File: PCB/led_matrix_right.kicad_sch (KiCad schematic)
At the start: 42 parts

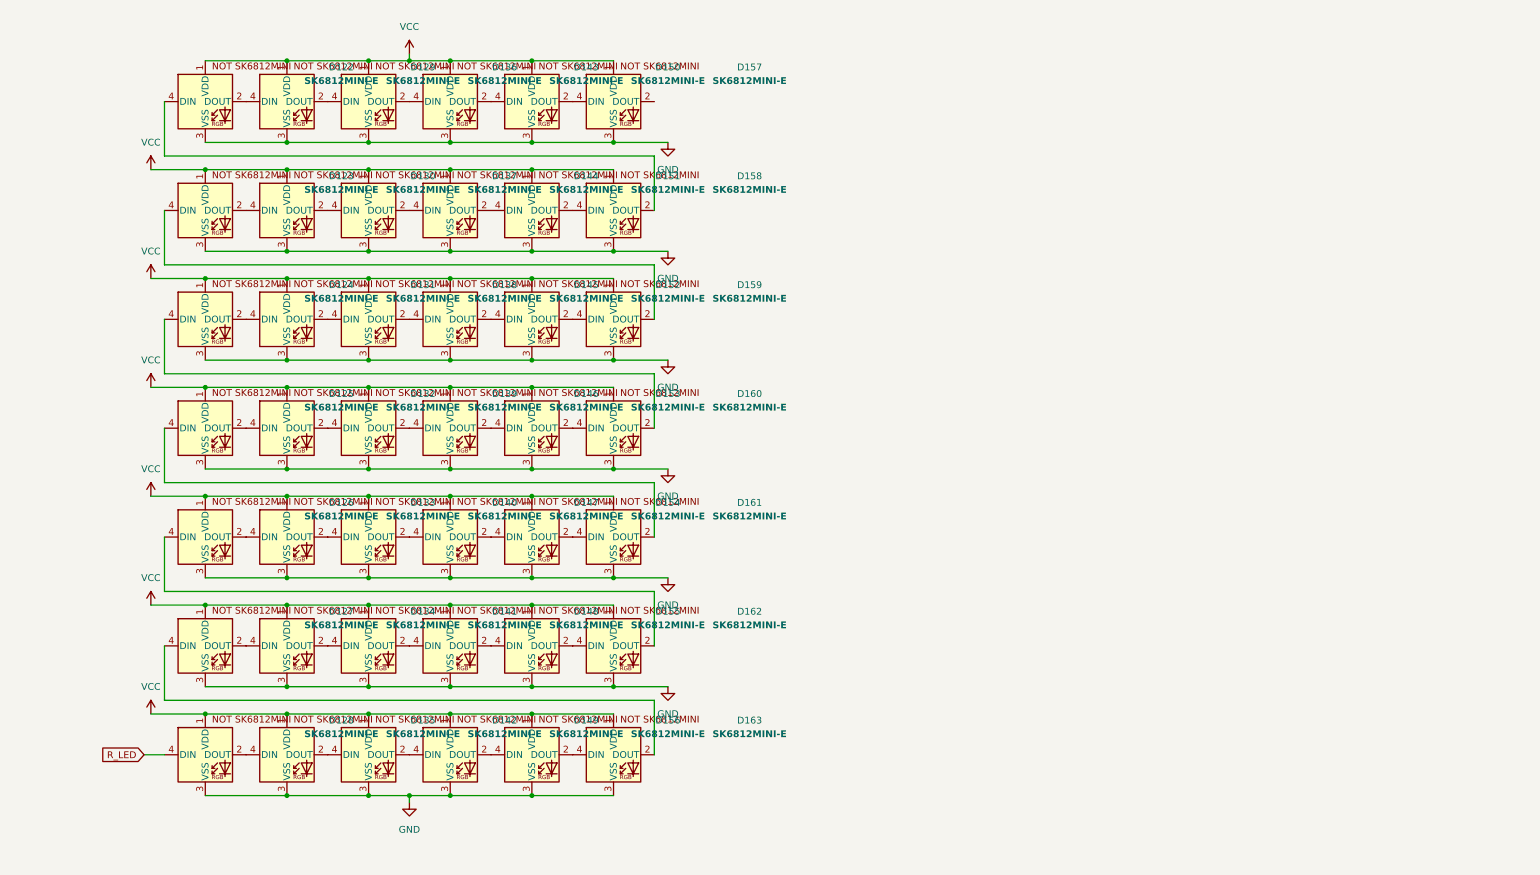
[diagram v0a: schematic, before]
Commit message: routed the switches and diodes
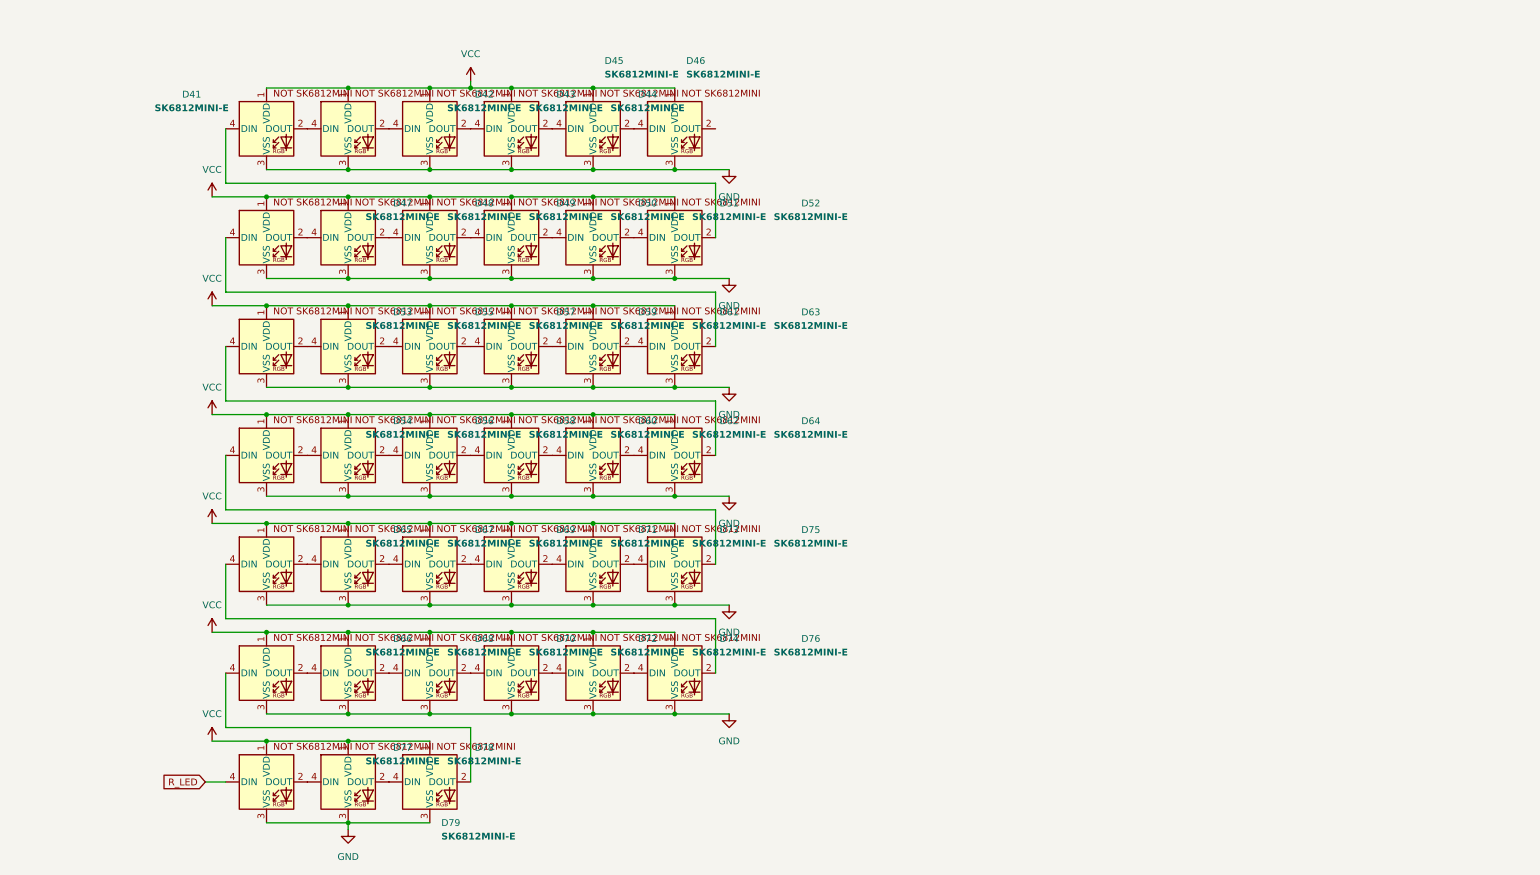
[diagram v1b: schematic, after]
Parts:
- removed D122, D123, D124, D125, D126, D127, D128, D129, D130, D131, D132, D133, D134, D135, D136, D137, D138, D139, D140, D141, D142, D143, D144, D145, D146, D147, D148, D149, D150, D151, D152, D153, D154, D155, D156, D157, D158, D159, D160, D161, D162, D163: SK6812MINI-E, footprints:SK6812MINI-E_fixed, symbol SK6812MINI-E:SK6812MINI-E
- added D41, D42, D43, D44, D45, D46, D47, D48, D49, D50, D51, D52, D53, D54, D55, D56, D57, D58, D59, D60, D61, D62, D63, D64, D65, D66, D67, D68, D69, D70, D71, D72, D73, D74, D75, D76, D77, D78, D79: SK6812MINI-E, footprints:SK6812MINI-E_fixed, symbol SK6812MINI-E:SK6812MINI-E
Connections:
- net GND: now also D41.3 (VSS), D42.3 (VSS), D43.3 (VSS), D44.3 (VSS), D45.3 (VSS), D46.3 (VSS), D47.3 (VSS), D48.3 (VSS), D49.3 (VSS), D50.3 (VSS), D51.3 (VSS), D52.3 (VSS), D53.3 (VSS), D54.3 (VSS), D55.3 (VSS), D56.3 (VSS), D57.3 (VSS), D58.3 (VSS), D59.3 (VSS), D60.3 (VSS), D61.3 (VSS), D62.3 (VSS), D63.3 (VSS), D64.3 (VSS), D65.3 (VSS), D66.3 (VSS), D67.3 (VSS), D68.3 (VSS), D69.3 (VSS), D70.3 (VSS), D71.3 (VSS), D72.3 (VSS), D73.3 (VSS), D74.3 (VSS), D75.3 (VSS), D76.3 (VSS), D77.3 (VSS), D78.3 (VSS), D79.3 (VSS)
- net R_LED: now also D77.4 (DIN)
- net VCC: now also D41.1 (VDD), D42.1 (VDD), D43.1 (VDD), D44.1 (VDD), D45.1 (VDD), D46.1 (VDD), D47.1 (VDD), D48.1 (VDD), D49.1 (VDD), D50.1 (VDD), D51.1 (VDD), D52.1 (VDD), D53.1 (VDD), D54.1 (VDD), D55.1 (VDD), D56.1 (VDD), D57.1 (VDD), D58.1 (VDD), D59.1 (VDD), D60.1 (VDD), D61.1 (VDD), D62.1 (VDD), D63.1 (VDD), D64.1 (VDD), D65.1 (VDD), D66.1 (VDD), D67.1 (VDD), D68.1 (VDD), D69.1 (VDD), D70.1 (VDD), D71.1 (VDD), D72.1 (VDD), D73.1 (VDD), D74.1 (VDD), D75.1 (VDD), D76.1 (VDD), D77.1 (VDD), D78.1 (VDD), D79.1 (VDD)
- new net: D66.2 (DOUT), D68.4 (DIN)
- new net: D66.4 (DIN), D79.2 (DOUT)
- new net: D65.4 (DIN), D76.2 (DOUT)
- new net: D74.2 (DOUT), D76.4 (DIN)
- new net: D71.2 (DOUT), D73.4 (DIN)
- new net: D69.2 (DOUT), D71.4 (DIN)
- new net: D62.2 (DOUT), D64.4 (DIN)
- new net: D60.2 (DOUT), D62.4 (DIN)
- new net: D78.2 (DOUT), D79.4 (DIN)
- new net: D47.2 (DOUT), D48.4 (DIN)
- new net: D47.4 (DIN), D63.2 (DOUT)
- new net: D53.4 (DIN), D64.2 (DOUT)
- new net: D70.2 (DOUT), D72.4 (DIN)
- new net: D68.2 (DOUT), D70.4 (DIN)
- new net: D73.2 (DOUT), D75.4 (DIN)
- new net: D67.2 (DOUT), D69.4 (DIN)
- new net: D61.2 (DOUT), D63.4 (DIN)
- new net: D58.2 (DOUT), D60.4 (DIN)
- new net: D56.2 (DOUT), D58.4 (DIN)
- new net: D55.2 (DOUT), D57.4 (DIN)
- new net: D53.2 (DOUT), D55.4 (DIN)
- new net: D59.2 (DOUT), D61.4 (DIN)
- new net: D57.2 (DOUT), D59.4 (DIN)
- new net: D45.2 (DOUT), D46.4 (DIN)
- new net: D44.2 (DOUT), D45.4 (DIN)
- new net: D43.2 (DOUT), D44.4 (DIN)
- new net: D72.2 (DOUT), D74.4 (DIN)
- new net: D54.2 (DOUT), D56.4 (DIN)
- new net: D42.2 (DOUT), D43.4 (DIN)
- new net: D41.2 (DOUT), D42.4 (DIN)
- new net: D49.2 (DOUT), D50.4 (DIN)
- new net: D48.2 (DOUT), D49.4 (DIN)
- new net: D41.4 (DIN), D52.2 (DOUT)
- new net: D51.2 (DOUT), D52.4 (DIN)
- new net: D65.2 (DOUT), D67.4 (DIN)
- new net: D77.2 (DOUT), D78.4 (DIN)
- new net: D54.4 (DIN), D75.2 (DOUT)
- new net: D50.2 (DOUT), D51.4 (DIN)

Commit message: redid the leds
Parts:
- removed D79: SK6812MINI-E, footprints:SK6812MINI-E_fixed, symbol SK6812MINI-E:SK6812MINI-E
- D41, D42, D43, D44, D45, D46, D47, D48, D49, D50, D51, D52, D53, D54, D55, D56, D57, D58, D59, D60, D61, D62, D63, D64, D65, D66, D67, D68, D69, D70, D71, D72, D73, D74, D75, D76, D77, D78: footprint footprints:SK6812MINI-E_fixed -> SK6812MINI-E - 3.2x2.8x1.78mm
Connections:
- net R_LED: now also D41.4 (DIN); no longer D77.4 (DIN)
- net at D66.2 (DOUT): now also D67.4 (DIN); no longer D68.4 (DIN)
- net at D66.4 (DIN): now also D65.2 (DOUT)
- net at D76.2 (DOUT): now also D77.4 (DIN); no longer D65.4 (DIN)
- net at D74.2 (DOUT): now also D75.4 (DIN); no longer D76.4 (DIN)
- net at D71.2 (DOUT): now also D72.4 (DIN); no longer D73.4 (DIN)
- net at D71.4 (DIN): now also D70.2 (DOUT); no longer D69.2 (DOUT)
- net at D64.4 (DIN): now also D63.2 (DOUT); no longer D62.2 (DOUT)
- net at D62.4 (DIN): now also D61.2 (DOUT); no longer D60.2 (DOUT)
- net at D47.4 (DIN): now also D46.2 (DOUT); no longer D63.2 (DOUT)
- net at D53.4 (DIN): now also D52.2 (DOUT); no longer D64.2 (DOUT)
- net at D70.4 (DIN): now also D69.2 (DOUT); no longer D68.2 (DOUT)
- net at D73.2 (DOUT): now also D74.4 (DIN); no longer D75.4 (DIN)
- net at D67.2 (DOUT): now also D68.4 (DIN); no longer D69.4 (DIN)
- net at D63.4 (DIN): now also D62.2 (DOUT); no longer D61.2 (DOUT)
- net at D58.2 (DOUT): now also D59.4 (DIN); no longer D60.4 (DIN)
- net at D56.2 (DOUT): now also D57.4 (DIN); no longer D58.4 (DIN)
- net at D55.2 (DOUT): now also D56.4 (DIN); no longer D57.4 (DIN)
- net at D55.4 (DIN): now also D54.2 (DOUT); no longer D53.2 (DOUT)
- net at D61.4 (DIN): now also D60.2 (DOUT); no longer D59.2 (DOUT)
- net at D57.2 (DOUT): now also D58.4 (DIN); no longer D59.4 (DIN)
- net at D72.2 (DOUT): now also D73.4 (DIN); no longer D74.4 (DIN)
- net at D75.2 (DOUT): now also D76.4 (DIN); no longer D54.4 (DIN)
- new net: D53.2 (DOUT), D54.4 (DIN)
- new net: D64.2 (DOUT), D65.4 (DIN)
- new net: D59.2 (DOUT), D60.4 (DIN)
- new net: D68.2 (DOUT), D69.4 (DIN)
- no-connect marks 0 -> 1

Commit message: "finished" right side
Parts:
- added D156: SK6812MINI-E, footprints:SK6812MINI-E_fixed, symbol SK6812MINI-E:SK6812MINI-E
- D41, D42, D43, D44, D45, D46, D47, D48, D49, D50, D51, D52, D53, D54, D55, D56, D57, D58, D59, D60, D61, D62, D63, D64, D65, D66, D67, D68, D69, D70, D71, D72, D73, D74, D75, D76, D77, D78: footprint SK6812MINI-E - 3.2x2.8x1.78mm -> footprints:SK6812MINI-E_fixed
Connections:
- net GND: now also D156.3 (VSS)
- net VCC: now also D156.1 (VDD)
- net at D78.2 (DOUT): now also D156.4 (DIN)
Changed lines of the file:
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@@
 	)
 	(junction
+		(at 125.73 62.23)
+		(diameter 0)
+		(color 0 0 0 0)
+	)
+	(junction
 		(at 140.97 16.51)
 		(diameter 0)
@@
 	)
 	(junction
+		(at 110.49 77.47)
+		(diameter 0)
+		(color 0 0 0 0)
+	)
+	(junction
 		(at 217.17 54.61)
 		(diameter 0)
@@
 	)
 	(no_connect
-		(at 118.11 69.85)
+		(at 133.35 69.85)
 	)
 	(wire
@@
 	(wire
 		(pts
+			(xy 125.73 62.23) (xy 110.49 62.23)
+		)
+		(stroke
+			(width 0)
+			(type default)
+		)
+	)
+	(wire
+		(pts
 			(xy 34.29 31.75) (xy 24.13 31.75)
 		)
@@
 	(wire
 		(pts
-			(xy 273.05 62.23) (xy 110.49 62.23)
+			(xy 273.05 62.23) (xy 125.73 62.23)
 		)
 		(stroke
@@
 	(wire
 		(pts
+			(xy 110.49 77.47) (xy 125.73 77.47)
+		)
+		(stroke
+			(width 0)
+			(type default)
+		)
+	)
+	(wire
+		(pts
 			(xy 171.45 39.37) (xy 186.69 39.37)
 		)
@@
 			)
 		)
-		(property "Footprint" "SK6812MINI-E - 3.2x2.8x1.78mm"
+		(property "Footprint" "footprints:SK6812MINI-E_fixed"
 			(at 111.76 77.47 0)
 			(effects
@@
 			)
 		)
-		(property "Footprint" "SK6812MINI-E - 3.2x2.8x1.78mm"
+		(property "Footprint" "footprints:SK6812MINI-E_fixed"
 			(at 264.16 31.75 0)
 			(effects
@@
 			)
 		)
-		(property "Footprint" "SK6812MINI-E - 3.2x2.8x1.78mm"
+		(property "Footprint" "footprints:SK6812MINI-E_fixed"
 			(at 50.8 54.61 0)
 			(effects
@@
 			)
 		)
-		(property "Footprint" "SK6812MINI-E - 3.2x2.8x1.78mm"
+		(property "Footprint" "footprints:SK6812MINI-E_fixed"
 			(at 66.04 31.75 0)
 			(effects
@@
 			)
 		)
-		(property "Footprint" "SK6812MINI-E - 3.2x2.8x1.78mm"
+		(property "Footprint" "footprints:SK6812MINI-E_fixed"
 			(at 111.76 31.75 0)
 			(effects
@@
 			)
 		)
-		(property "Footprint" "SK6812MINI-E - 3.2x2.8x1.78mm"
+		(property "Footprint" "footprints:SK6812MINI-E_fixed"
 			(at 96.52 54.61 0)
 			(effects
@@
 			)
 		)
-		(property "Footprint" "SK6812MINI-E - 3.2x2.8x1.78mm"
+		(property "Footprint" "footprints:SK6812MINI-E_fixed"
 			(at 142.24 31.75 0)
 			(effects
@@
 			)
 		)
-		(property "Footprint" "SK6812MINI-E - 3.2x2.8x1.78mm"
+		(property "Footprint" "footprints:SK6812MINI-E_fixed"
 			(at 157.48 31.75 0)
 			(effects
@@
 			)
 		)
-		(property "Footprint" "SK6812MINI-E - 3.2x2.8x1.78mm"
+		(property "Footprint" "footprints:SK6812MINI-E_fixed"
 			(at 96.52 31.75 0)
 			(effects
@@
 			)
 		)
-		(property "Footprint" "SK6812MINI-E - 3.2x2.8x1.78mm"
+		(property "Footprint" "footprints:SK6812MINI-E_fixed"
 			(at 35.56 31.75 0)
 			(effects
@@
 			)
 		)
-		(property "Footprint" "SK6812MINI-E - 3.2x2.8x1.78mm"
+		(property "Footprint" "footprints:SK6812MINI-E_fixed"
 			(at 50.8 77.47 0)
 			(effects
@@
 			)
 		)
-		(property "Footprint" "SK6812MINI-E - 3.2x2.8x1.78mm"
+		(property "Footprint" "footprints:SK6812MINI-E_fixed"
 			(at 81.28 77.47 0)
 			(effects
@@
 			)
 		)
-		(property "Footprint" "SK6812MINI-E - 3.2x2.8x1.78mm"
+		(property "Footprint" "footprints:SK6812MINI-E_fixed"
 			(at 248.92 54.61 0)
 			(effects
@@
 			)
 		)
-		(property "Footprint" "SK6812MINI-E - 3.2x2.8x1.78mm"
+		(property "Footprint" "footprints:SK6812MINI-E_fixed"
 			(at 203.2 31.75 0)
 			(effects
@@
 			)
 		)
-		(property "Footprint" "SK6812MINI-E - 3.2x2.8x1.78mm"
+		(property "Footprint" "footprints:SK6812MINI-E_fixed"
 			(at 233.68 31.75 0)
 			(effects
@@
 			)
 		)
-		(property "Footprint" "SK6812MINI-E - 3.2x2.8x1.78mm"
+		(property "Footprint" "footprints:SK6812MINI-E_fixed"
 			(at 50.8 31.75 0)
 			(effects
@@
 			)
 		)
-		(property "Footprint" "SK6812MINI-E - 3.2x2.8x1.78mm"
+		(property "Footprint" "footprints:SK6812MINI-E_fixed"
 			(at 35.56 77.47 0)
 			(effects
@@
 			)
 		)
-		(property "Footprint" "SK6812MINI-E - 3.2x2.8x1.78mm"
+		(property "Footprint" "footprints:SK6812MINI-E_fixed"
 			(at 142.24 54.61 0)
 			(effects
@@
 			)
 		)
-		(property "Footprint" "SK6812MINI-E - 3.2x2.8x1.78mm"
+		(property "Footprint" "footprints:SK6812MINI-E_fixed"
 			(at 233.68 54.61 0)
 			(effects
@@
 			)
 		)
-		(property "Footprint" "SK6812MINI-E - 3.2x2.8x1.78mm"
+		(property "Footprint" "footprints:SK6812MINI-E_fixed"
 			(at 81.28 54.61 0)
 			(effects
@@
 			)
 		)
-		(property "Footprint" "SK6812MINI-E - 3.2x2.8x1.78mm"
+		(property "Footprint" "footprints:SK6812MINI-E_fixed"
 			(at 218.44 31.75 0)
 			(effects
@@
 			)
 		)
-		(property "Footprint" "SK6812MINI-E - 3.2x2.8x1.78mm"
+		(property "Footprint" "footprints:SK6812MINI-E_fixed"
 			(at 81.28 31.75 0)
 			(effects
@@
 			)
 		)
-		(property "Footprint" "SK6812MINI-E - 3.2x2.8x1.78mm"
+		(property "Footprint" "footprints:SK6812MINI-E_fixed"
 			(at 35.56 54.61 0)
 			(effects
@@
 	(symbol
 		(lib_id "SK6812MINI-E:SK6812MINI-E")
+		(at 125.73 69.85 0)
+		(unit 1)
+		(exclude_from_sim no)
+		(in_bom yes)
+		(on_board yes)
+		(dnp no)
+		(property "Reference" "D156"
+			(at 151.638 63.5 0)
+			(effects
+				(font
+					(size 1.27 1.27)
+				)
+			)
+		)
+		(property "Value" "SK6812MINI-E"
+			(at 151.13 65.9699 0)
+			(effects
+				(font
+					(size 1.27 1.27)
+					(thickness 0.254)
+					(bold yes)
+				)
+			)
+		)
+		(property "Footprint" "footprints:SK6812MINI-E_fixed"
+			(at 127 77.47 0)
+			(effects
+				(font
+					(size 1.27 1.27)
+				)
+				(justify left top)
+				(hide yes)
+			)
+		)
+		(property "Datasheet" "https://cdn-shop.adafruit.com/product-files/4960/4960_SK6812MINI-E_REV02_EN.pdf"
+			(at 128.27 79.375 0)
+			(effects
+				(font
+					(size 1.27 1.27)
+				)
+				(justify left top)
+				(hide yes)
+			)
+		)
+		(property "Description" "RGB LED with integrated controller"
+			(at 125.73 69.85 0)
+			(effects
+				(font
+					(size 1.27 1.27)
+				)
+				(hide yes)
+			)
+		)
+		(pin "2"
+		)
+		(pin "1"
+		)
+		(pin "3"
+		)
+		(pin "4"
+		)
+		(instances
+			(project "split_keeb"
+				(path "/b7eb43b0-c363-4b01-b49e-ca46ab5210f5/ac7847d3-359c-4738-8c91-d422e2327a5e/7592b499-08d9-43f7-bbee-81726890c12e"
+					(reference "D156")
+					(unit 1)
+				)
+			)
+		)
+	)
+	(symbol
+		(lib_id "SK6812MINI-E:SK6812MINI-E")
 		(at 247.65 24.13 0)
 		(unit 1)
@@
 			)
 		)
-		(property "Footprint" "SK6812MINI-E - 3.2x2.8x1.78mm"
+		(property "Footprint" "footprints:SK6812MINI-E_fixed"
 			(at 248.92 31.75 0)
 			(effects
@@
 			)
 		)
-		(property "Footprint" "SK6812MINI-E - 3.2x2.8x1.78mm"
+		(property "Footprint" "footprints:SK6812MINI-E_fixed"
 			(at 157.48 54.61 0)
 			(effects
@@
 			)
 		)
-		(property "Footprint" "SK6812MINI-E - 3.2x2.8x1.78mm"
+		(property "Footprint" "footprints:SK6812MINI-E_fixed"
 			(at 264.16 54.61 0)
 			(effects
@@
 			)
 		)
-		(property "Footprint" "SK6812MINI-E - 3.2x2.8x1.78mm"
+		(property "Footprint" "footprints:SK6812MINI-E_fixed"
 			(at 172.72 54.61 0)
 			(effects
@@
 			)
 		)
-		(property "Footprint" "SK6812MINI-E - 3.2x2.8x1.78mm"
+		(property "Footprint" "footprints:SK6812MINI-E_fixed"
 			(at 187.96 31.75 0)
 			(effects
@@
 			)
 		)
-		(property "Footprint" "SK6812MINI-E - 3.2x2.8x1.78mm"
+		(property "Footprint" "footprints:SK6812MINI-E_fixed"
 			(at 172.72 31.75 0)
 			(effects
@@
 			)
 		)
-		(property "Footprint" "SK6812MINI-E - 3.2x2.8x1.78mm"
+		(property "Footprint" "footprints:SK6812MINI-E_fixed"
 			(at 127 54.61 0)
 			(effects
@@
 			)
 		)
-		(property "Footprint" "SK6812MINI-E - 3.2x2.8x1.78mm"
+		(property "Footprint" "footprints:SK6812MINI-E_fixed"
 			(at 66.04 77.47 0)
 			(effects
@@
 			)
 		)
-		(property "Footprint" "SK6812MINI-E - 3.2x2.8x1.78mm"
+		(property "Footprint" "footprints:SK6812MINI-E_fixed"
 			(at 187.96 54.61 0)
 			(effects
@@
 			)
 		)
-		(property "Footprint" "SK6812MINI-E - 3.2x2.8x1.78mm"
+		(property "Footprint" "footprints:SK6812MINI-E_fixed"
 			(at 203.2 54.61 0)
 			(effects
@@
 			)
 		)
-		(property "Footprint" "SK6812MINI-E - 3.2x2.8x1.78mm"
+		(property "Footprint" "footprints:SK6812MINI-E_fixed"
 			(at 66.04 54.61 0)
 			(effects
@@
 			)
 		)
-		(property "Footprint" "SK6812MINI-E - 3.2x2.8x1.78mm"
+		(property "Footprint" "footprints:SK6812MINI-E_fixed"
 			(at 127 31.75 0)
 			(effects
@@
 			)
 		)
-		(property "Footprint" "SK6812MINI-E - 3.2x2.8x1.78mm"
+		(property "Footprint" "footprints:SK6812MINI-E_fixed"
 			(at 96.52 77.47 0)
 			(effects
@@
 			)
 		)
-		(property "Footprint" "SK6812MINI-E - 3.2x2.8x1.78mm"
+		(property "Footprint" "footprints:SK6812MINI-E_fixed"
 			(at 218.44 54.61 0)
 			(effects
@@
 			)
 		)
-		(property "Footprint" "SK6812MINI-E - 3.2x2.8x1.78mm"
+		(property "Footprint" "footprints:SK6812MINI-E_fixed"
 			(at 111.76 54.61 0)
 			(effects
